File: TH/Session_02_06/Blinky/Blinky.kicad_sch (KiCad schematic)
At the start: 13 parts, among them SW1 SW_SPDT, U1 TLC551CD‎

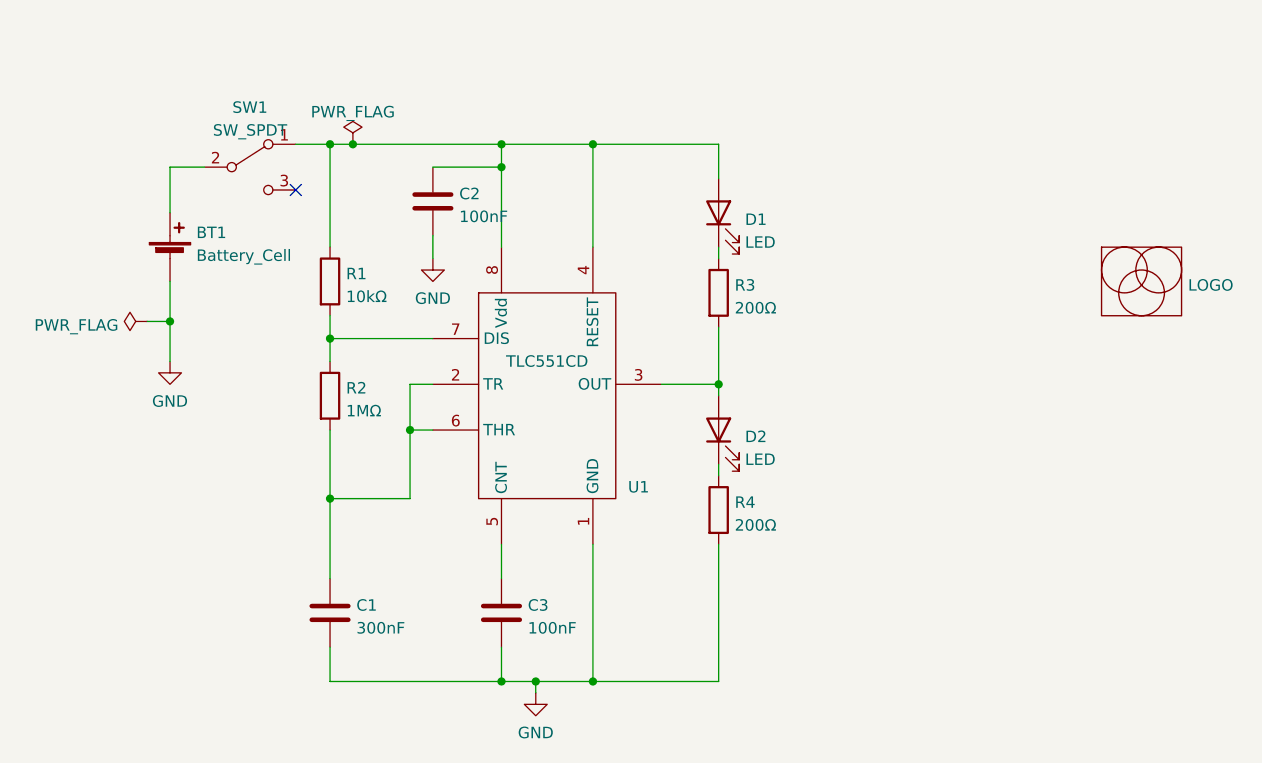
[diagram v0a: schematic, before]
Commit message: Revamps the through-hole project as transistor based
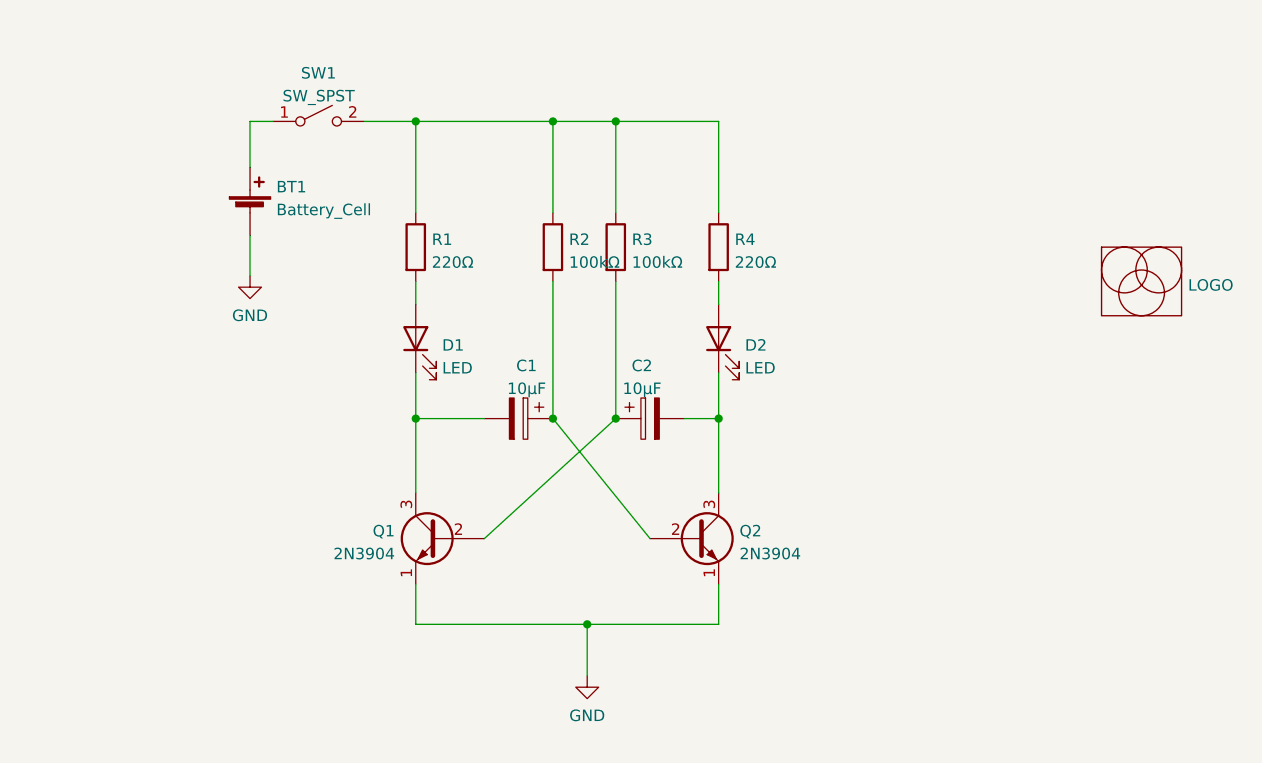
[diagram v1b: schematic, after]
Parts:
- removed C1: 300nF, Capacitor_THT:C_Disc_D5.0mm_W2.5mm_P5.00mm, symbol Device:C
- removed C2, C3: 100nF, Capacitor_THT:C_Disc_D5.0mm_W2.5mm_P5.00mm, symbol Device:C
- removed SW1: SW_SPDT, Blinky_ZAM:SSK-1202, symbol Switch:SW_SPDT
- removed U1: TLC551CD‎, Package_DIP:DIP-8_W7.62mm_Socket, symbol Blinky:TLC551CD‎
- added C1, C2: 10μF, Capacitor_THT:CP_Radial_D5.0mm_P2.50mm, symbol Device:C_Polarized
- added Q1, Q2: 2N3904, Package_TO_SOT_THT:TO-92_Inline, symbol Transistor_BJT:2N3904
- added SW1: SW_SPST, Blinky_ZAM:SSK-1202, symbol Switch:SW_SPST
- LG2: footprint Blinky_ZAM:ZAM_LOGO_440 -> Blinky_ZAM:ZAM_LOGO_440_stopMask
- R1: value 10kΩ -> 220Ω; footprint Resistor_THT:R_Axial_DIN0207_L6.3mm_D2.5mm_P10.16mm_Horizontal -> Resistor_THT:R_Axial_DIN0207_L6.3mm_D2.5mm_P2.54mm_Vertical
- R2: value 1MΩ -> 100kΩ; footprint Resistor_THT:R_Axial_DIN0207_L6.3mm_D2.5mm_P10.16mm_Horizontal -> Resistor_THT:R_Axial_DIN0207_L6.3mm_D2.5mm_P2.54mm_Vertical
- R3: value 200Ω -> 100kΩ; footprint Resistor_THT:R_Axial_DIN0207_L6.3mm_D2.5mm_P10.16mm_Horizontal -> Resistor_THT:R_Axial_DIN0207_L6.3mm_D2.5mm_P2.54mm_Vertical
- R4: value 200Ω -> 220Ω; footprint Resistor_THT:R_Axial_DIN0207_L6.3mm_D2.5mm_P10.16mm_Horizontal -> Resistor_THT:R_Axial_DIN0207_L6.3mm_D2.5mm_P2.54mm_Vertical
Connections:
- net GND: now also Q1.1 (E), Q2.1 (E); no longer R4.2
- net at R2.2: now also C1.1, Q2.2 (B)
- net at R3.2: now also C2.1, Q1.2 (B); no longer D2.2 (A)
- net at R1.1: now also R2.1, R3.1, R4.1, SW1.2 (B); no longer D1.2 (A)
- net at R1.2: now also D1.2 (A); no longer R2.1
- net at D2.1 (K): now also C2.2, Q2.3 (C); no longer R4.1
- net at D1.1 (K): now also C1.2, Q1.3 (C); no longer R3.1
- net at BT1.1 (+): now also SW1.1 (A)
- new net: D2.2 (A), R4.2
- no-connect marks 1 -> 0

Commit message: Makes corrections to the design rules
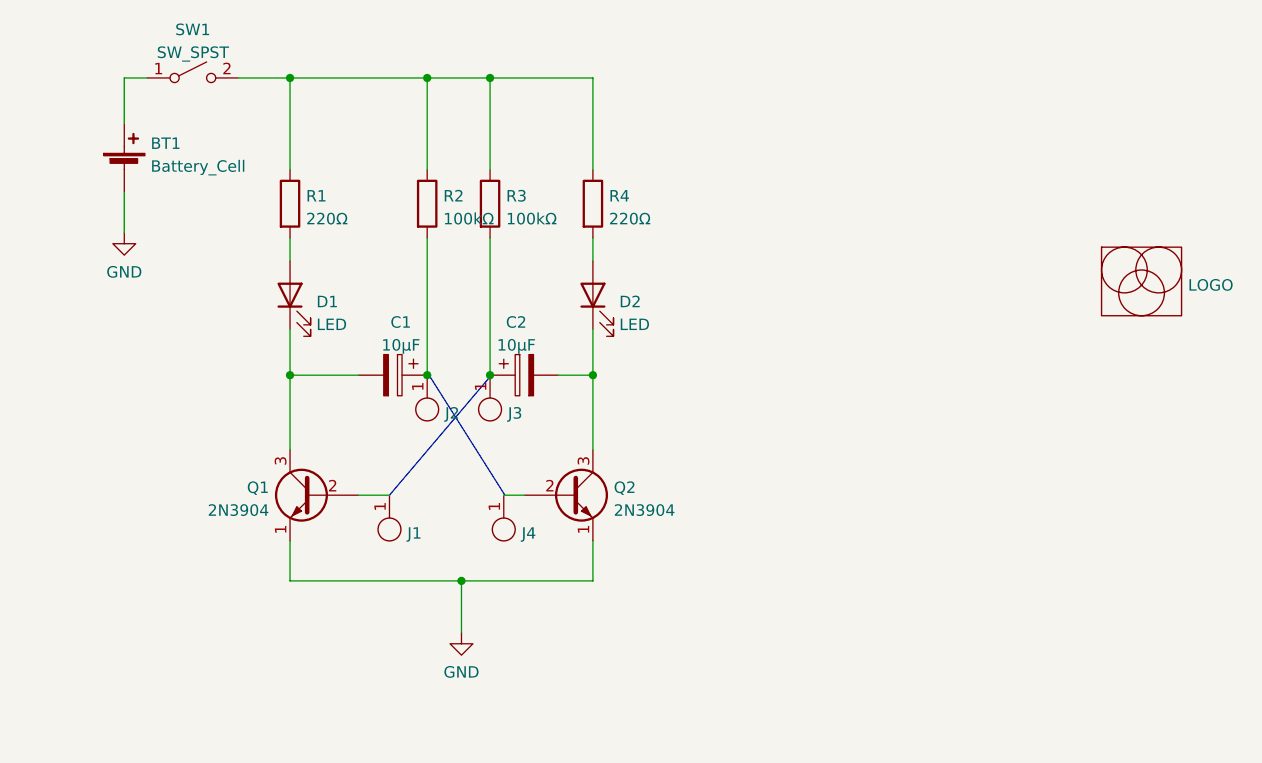
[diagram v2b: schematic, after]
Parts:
- added J1, J2, J3, J4: Jumper_1, TestPoint:TestPoint_THTPad_2.0x2.0mm_Drill1.0mm, symbol Blinky:Jumper_1
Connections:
- net at C2.1, R3.2: now also J3.1; no longer Q1.2 (B)
- net at C1.1, R2.2: now also J2.1; no longer Q2.2 (B)
- new net: J4.1, Q2.2 (B)
- new net: J1.1, Q1.2 (B)

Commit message: For the BOM
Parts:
- J1, J2, J4: value Jumper_1 -> bridge
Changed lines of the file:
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@@
       (effects (font (size 1.27 1.27)) (justify right))
     )
-    (property "Value" "Jumper_1" (id 1) (at 95.885 68.834 0)
+    (property "Value" "bridge" (id 1) (at 95.885 68.834 0)
       (effects (font (size 1.27 1.27)) hide)
     )
@@
       (effects (font (size 1.27 1.27)) (justify right))
     )
-    (property "Value" "Jumper_1" (id 1) (at 102.87 68.834 0)
+    (property "Value" "bridge" (id 1) (at 102.87 68.834 0)
       (effects (font (size 1.27 1.27)) hide)
     )
@@
       (effects (font (size 1.27 1.27)) (justify right))
     )
-    (property "Value" "Jumper_1" (id 1) (at 104.394 82.169 0)
+    (property "Value" "bridge" (id 1) (at 104.394 82.169 0)
       (effects (font (size 1.27 1.27)) hide)
     )
@@
       (effects (font (size 1.27 1.27)) (justify right))
     )
-    (property "Value" "Jumper_1" (id 1) (at 91.694 82.169 0)
+    (property "Value" "bridge" (id 1) (at 91.694 82.169 0)
       (effects (font (size 1.27 1.27)) hide)
     )
@@
     )
     (path "/ce77231a-317e-46f7-a29d-b51fb31df2af"
-      (reference "J1") (unit 1) (value "Jumper_1") (footprint "TestPoint:TestPoint_THTPad_2.0x2.0mm_Drill1.0mm")
+      (reference "J1") (unit 1) (value "bridge") (footprint "TestPoint:TestPoint_THTPad_2.0x2.0mm_Drill1.0mm")
     )
     (path "/12e5d3a6-a076-4711-919f-81dc93d0c2fd"
-      (reference "J2") (unit 1) (value "Jumper_1") (footprint "TestPoint:TestPoint_THTPad_2.0x2.0mm_Drill1.0mm")
+      (reference "J2") (unit 1) (value "bridge") (footprint "TestPoint:TestPoint_THTPad_2.0x2.0mm_Drill1.0mm")
     )
     (path "/4b8ea50e-bc5f-4e52-bf91-1f55d8bf0549"
-      (reference "J3") (unit 1) (value "Jumper_1") (footprint "TestPoint:TestPoint_THTPad_2.0x2.0mm_Drill1.0mm")
+      (reference "J3") (unit 1) (value "bridge") (footprint "TestPoint:TestPoint_THTPad_2.0x2.0mm_Drill1.0mm")
     )
     (path "/c1cbda1b-2305-4d97-8468-1a6bed162811"
-      (reference "J4") (unit 1) (value "Jumper_1") (footprint "TestPoint:TestPoint_THTPad_2.0x2.0mm_Drill1.0mm")
+      (reference "J4") (unit 1) (value "bridge") (footprint "TestPoint:TestPoint_THTPad_2.0x2.0mm_Drill1.0mm")
     )
     (path "/46c4f0f5-7d12-4715-a65e-56070cb3016e"

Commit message: Correction to the NPN symbol to the purchased part Session_02_06 only
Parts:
- removed Q1, Q2: 2N3904, Package_TO_SOT_THT:TO-92_Inline, symbol Transistor_BJT:2N3904
- added Q1, Q2: 2N3904, Package_TO_SOT_THT:TO-92_Inline, symbol Blinky:2N3904
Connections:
- net GND: now also Q1.3 (E), Q2.3 (E)
- net at C2.2, D2.1 (K): now also Q2.1 (C)
- net at C1.2, D1.1 (K): now also Q1.1 (C)
- net at J4.1: now also Q2.2 (B)
- net at J1.1: now also Q1.2 (B)
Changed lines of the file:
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@@
     (pin "2")
+  )
+  (symbol (lib_id "Blinky:2N3904") (at 114.3 78.359 0) (unit 1)
+    (in_bom yes) (on_board yes) (fields_autoplaced)
+    (property "Reference" "Q2" (id 0) (at 119.1514 77.5243 0)
+      (effects (font (size 1.27 1.27)) (justify left))
+    )
+    (property "Value" "2N3904" (id 1) (at 119.1514 80.0612 0)
+      (effects (font (size 1.27 1.27)) (justify left))
+    )
+    (property "Footprint" "Package_TO_SOT_THT:TO-92_Inline" (id 2) (at 119.38 80.264 0)
+      (effects (font (size 1.27 1.27) italic) (justify left) hide)
+    )
+    (property "Datasheet" "https://www.onsemi.com/pub/Collateral/2N3903-D.PDF" (id 3) (at 114.3 78.359 0)
+      (effects (font (size 1.27 1.27)) (justify left) hide)
+    )
+    (pin "1")
+    (pin "2")
+    (pin "3")
   )
   (symbol (lib_id "Blinky:Jumper_1") (at 98.425 68.834 90) (unit 1)
@@
     (pin "2")
   )
+  (symbol (lib_id "Blinky:2N3904") (at 85.725 78.359 0) (mirror y) (unit 1)
+    (in_bom yes) (on_board yes) (fields_autoplaced)
+    (property "Reference" "Q1" (id 0) (at 80.8737 77.5243 0)
+      (effects (font (size 1.27 1.27)) (justify left))
+    )
+    (property "Value" "2N3904" (id 1) (at 80.8737 80.0612 0)
+      (effects (font (size 1.27 1.27)) (justify left))
+    )
+    (property "Footprint" "Package_TO_SOT_THT:TO-92_Inline" (id 2) (at 80.645 80.264 0)
+      (effects (font (size 1.27 1.27) italic) (justify left) hide)
+    )
+    (property "Datasheet" "https://www.onsemi.com/pub/Collateral/2N3903-D.PDF" (id 3) (at 85.725 78.359 0)
+      (effects (font (size 1.27 1.27)) (justify left) hide)
+    )
+    (pin "1")
+    (pin "2")
+    (pin "3")
+  )
   (symbol (lib_id "Device:R") (at 83.185 45.974 0) (unit 1)
     (in_bom yes) (on_board yes) (fields_autoplaced)
@@
     (pin "1")
   )
-  (symbol (lib_id "Transistor_BJT:2N3904") (at 85.725 78.359 0) (mirror y) (unit 1)
-    (in_bom yes) (on_board yes) (fields_autoplaced)
-    (property "Reference" "Q1" (id 0) (at 80.8737 77.5243 0)
-      (effects (font (size 1.27 1.27)) (justify left))
-    )
-    (property "Value" "2N3904" (id 1) (at 80.8737 80.0612 0)
-      (effects (font (size 1.27 1.27)) (justify left))
-    )
-    (property "Footprint" "Package_TO_SOT_THT:TO-92_Inline" (id 2) (at 80.645 80.264 0)
-      (effects (font (size 1.27 1.27) italic) (justify left) hide)
-    )
-    (property "Datasheet" "https://www.onsemi.com/pub/Collateral/2N3903-D.PDF" (id 3) (at 85.725 78.359 0)
-      (effects (font (size 1.27 1.27)) (justify left) hide)
-    )
-    (pin "1")
-    (pin "2")
-    (pin "3")
-  )
   (symbol (lib_id "power:GND") (at 64.77 49.149 0) (unit 1)
     (in_bom yes) (on_board yes) (fields_autoplaced)
@@
     )
     (pin "1")
-  )
-  (symbol (lib_id "Transistor_BJT:2N3904") (at 114.3 78.359 0) (unit 1)
-    (in_bom yes) (on_board yes) (fields_autoplaced)
-    (property "Reference" "Q2" (id 0) (at 119.1514 77.5243 0)
-      (effects (font (size 1.27 1.27)) (justify left))
-    )
-    (property "Value" "2N3904" (id 1) (at 119.1514 80.0612 0)
-      (effects (font (size 1.27 1.27)) (justify left))
-    )
-    (property "Footprint" "Package_TO_SOT_THT:TO-92_Inline" (id 2) (at 119.38 80.264 0)
-      (effects (font (size 1.27 1.27) italic) (justify left) hide)
-    )
-    (property "Datasheet" "https://www.onsemi.com/pub/Collateral/2N3903-D.PDF" (id 3) (at 114.3 78.359 0)
-      (effects (font (size 1.27 1.27)) (justify left) hide)
-    )
-    (pin "1")
-    (pin "2")
-    (pin "3")
   )
   (symbol (lib_id "Device:Battery_Cell") (at 64.77 42.164 0) (unit 1)
@@
       (reference "LG2") (unit 1) (value "LOGO") (footprint "Blinky_ZAM:ZAM_LOGO_440_stopMask")
     )
-    (path "/d231b70d-8a29-4e78-a17c-75abb025b07e"
+    (path "/accca145-7a6d-4ae5-be19-139ea3b35077"
       (reference "Q1") (unit 1) (value "2N3904") (footprint "Package_TO_SOT_THT:TO-92_Inline")
     )
-    (path "/ed8cae4f-91dd-4b4e-8735-82d1cba8a90d"
+    (path "/0d357f9e-b819-47a4-b1c7-9f5c343775ea"
       (reference "Q2") (unit 1) (value "2N3904") (footprint "Package_TO_SOT_THT:TO-92_Inline")
     )
